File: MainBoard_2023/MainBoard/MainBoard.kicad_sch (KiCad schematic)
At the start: 27 parts

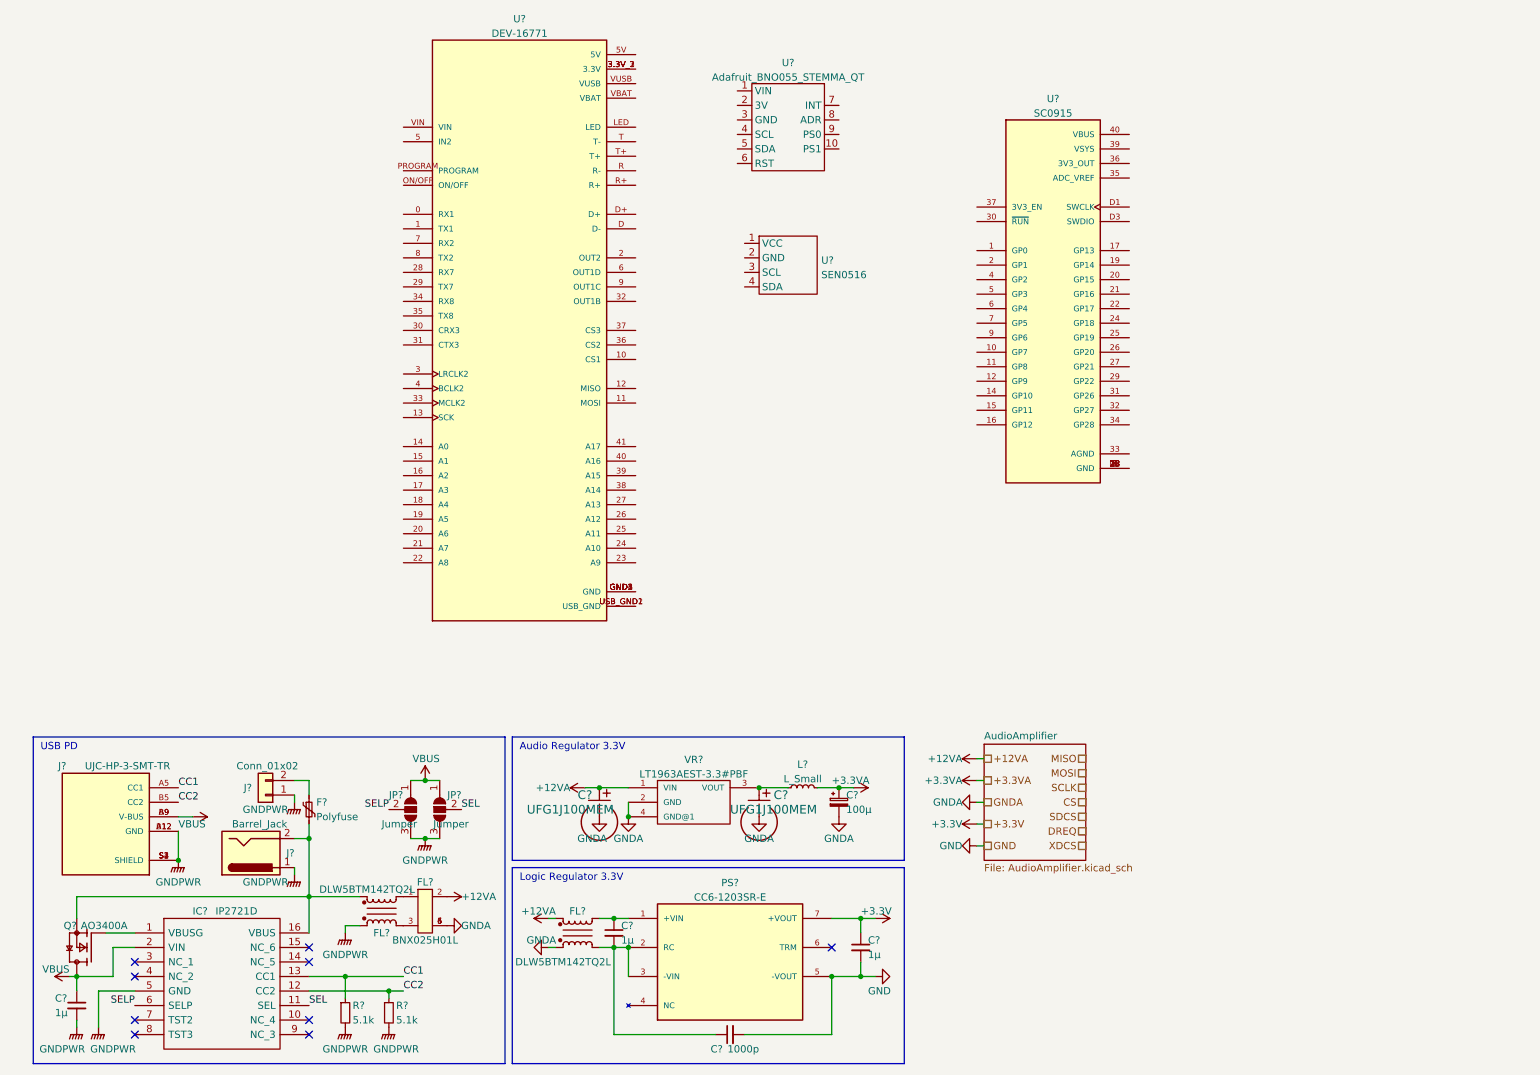
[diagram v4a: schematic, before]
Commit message: RS485回路を追加
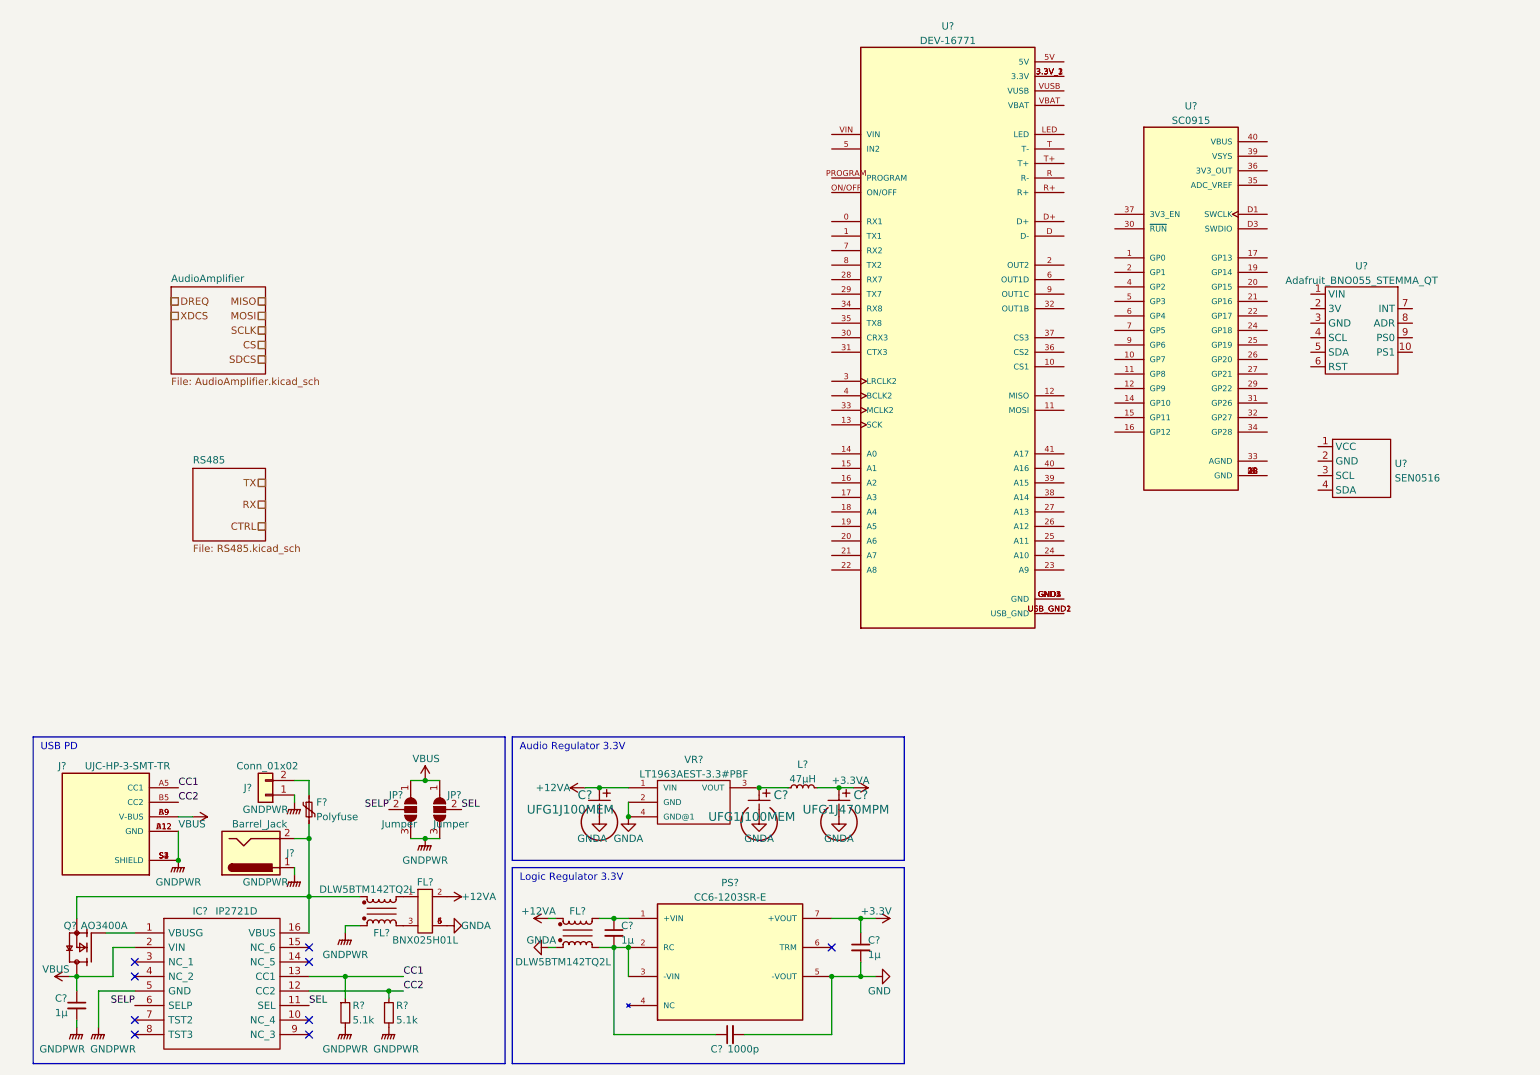
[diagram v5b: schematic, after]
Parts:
- removed C?: 100μ, symbol Device:C_Polarized_Small
- added C?: UFG1J470MPM, PCAP_10x12_5-THRU-ELECT_NCA, symbol UFG1J470MPM:UFG1J470MPM
- L?: value L_Small -> 47μH
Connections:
- net +3.3VA: now also C?.1
- net GNDA: now also C?.2
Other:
- added sheet RS485 (RS485.kicad_sch)
- moved on the sheet: U?

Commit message: picoのピンを設定
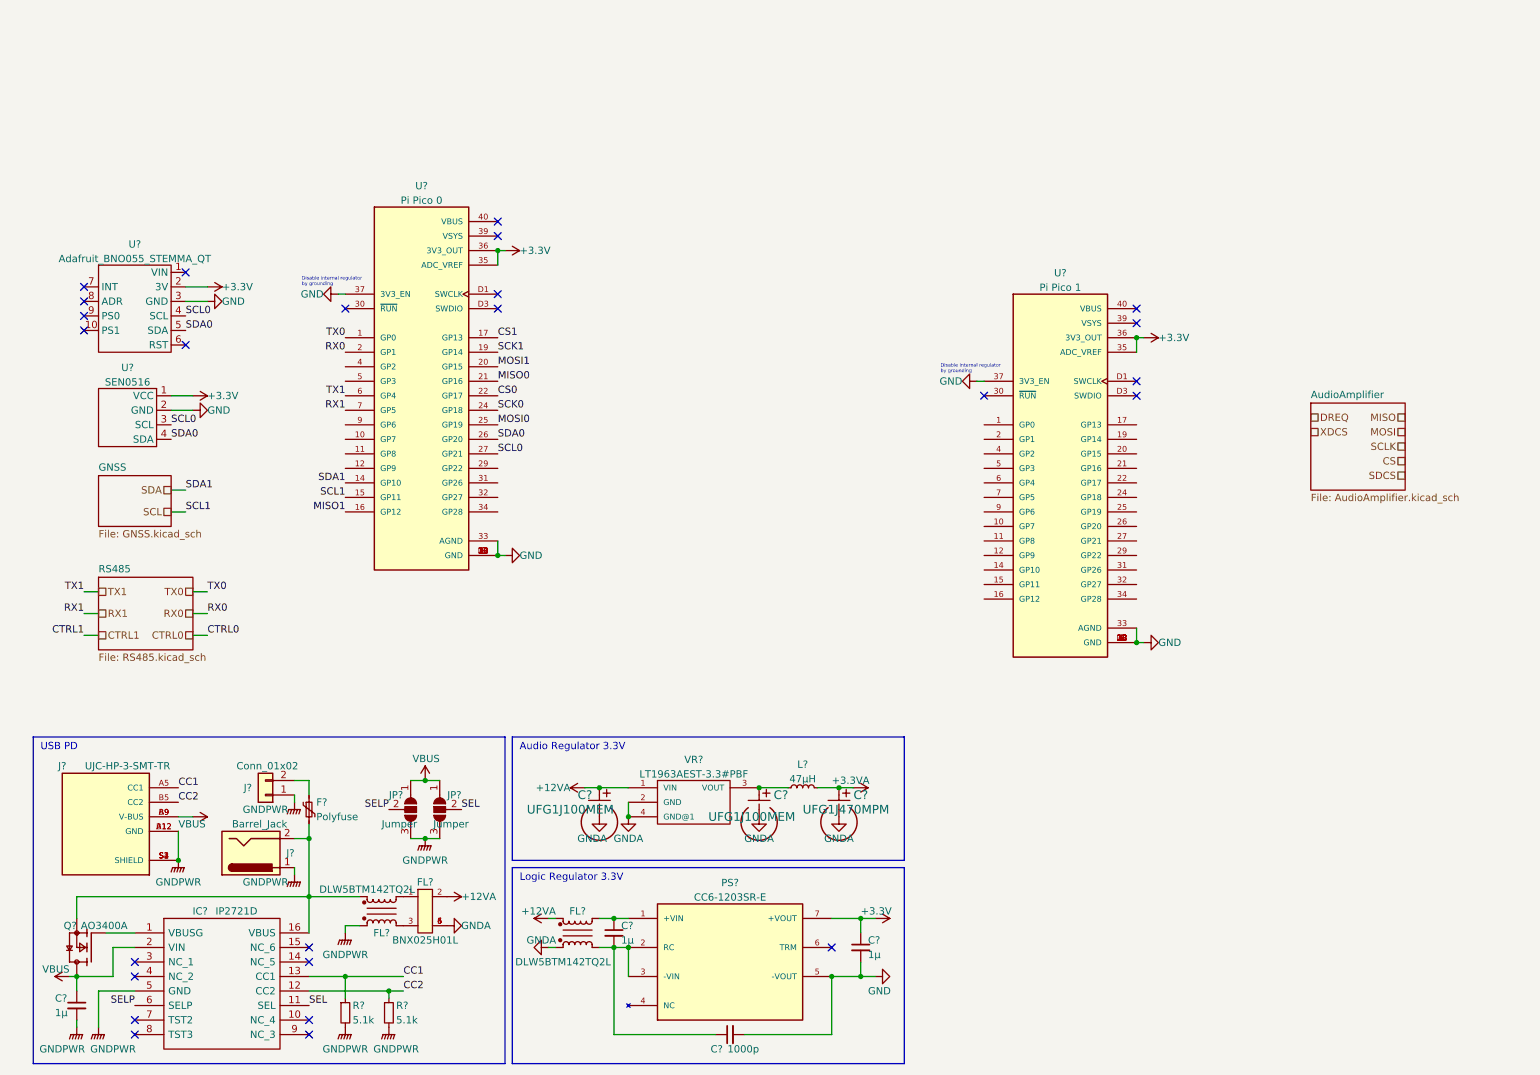
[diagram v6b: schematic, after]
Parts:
- removed U?: DEV-16771, MODULE_DEV-16771, symbol Teensy_4_1:DEV-16771
- removed U?: SC0915, MODULE_SC0915, symbol Raspberry_Pi_Pico:SC0915
- added U?: Pi Pico 0, MODULE_SC0915, symbol Raspberry_Pi_Pico:SC0915
- added U?: Pi Pico 1, MODULE_SC0915, symbol Raspberry_Pi_Pico:SC0915
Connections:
- net +3.3V: now also U?.1 (VCC), U?.2 (3V), U?.35 (ADC_VREF), U?.35 (ADC_VREF), U?.36 (3V3_OUT), U?.36 (3V3_OUT)
- net GND: now also U?.2 (GND), U?.3 (GND), U?.13 (GND), U?.13 (GND), U?.18 (GND), U?.18 (GND), U?.23 (GND), U?.23 (GND), U?.28 (GND), U?.28 (GND), U?.3 (GND), U?.3 (GND), U?.33 (AGND), U?.33 (AGND), U?.37 (3V3_EN), U?.37 (3V3_EN), U?.38 (GND), U?.38 (GND), U?.8 (GND), U?.8 (GND), U?.D2 (GND), U?.D2 (GND)
- net SCL0: now reaches U?.4 (SCL)
- net SCL0: now also U?.3 (SCL), U?.27 (GP21)
- net SDA0: now reaches U?.5 (SDA)
- net SDA0: now also U?.4 (SDA), U?.26 (GP20)
- new net CS0: U?.22 (GP17)
- new net CS1: U?.17 (GP13)
- new net MISO0: U?.21 (GP16)
- new net MISO1: U?.16 (GP12)
- new net MOSI0: U?.25 (GP19)
- new net MOSI1: U?.20 (GP15)
- new net RX0: U?.2 (GP1)
- new net RX1: U?.7 (GP5)
- new net SCK0: U?.24 (GP18)
- new net SCK1: U?.19 (GP14)
- new net SCL: U?.15 (GP11)
- new net SDA: U?.14 (GP10)
- new net TX0: U?.1 (GP0)
- new net TX1: U?.6 (GP4)
- no-connect marks 9 -> 25
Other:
- added sheet GNSS (GNSS.kicad_sch)
- note added: "Disable internal regulator by grounding"
- moved on the sheet: U?

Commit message: pico*2の場合
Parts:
- added C? (x2): 4.7μ, symbol Device:C_Small
- added C? (x2): 0.1μ, symbol Device:C_Small
- added J? (x2): Micro_SD_Card_Det_Hirose_DM3AT, symbol Connector:Micro_SD_Card_Det_Hirose_DM3AT
- added R? (x10): 10k, symbol Device:R_Small
- added R? (x2): 33, symbol Device:R_Small
- added U?: Seeed_Studio_XIAO_nRF52840_Sense, symbol Seeed_Studio_XIAO_nRF52840_Sense:Seeed_Studio_XIAO_nRF52840_Sense
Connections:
- net +3.3V: now also C?.1, C?.1, C?.1, C?.1, J?.4 (VDD), J?.4 (VDD), R?.2, R?.2, R?.2, R?.2, R?.2, R?.2, R?.2, R?.2, R?.2, R?.2, U?.12 (3V3)
- net CS0: now also J?.2 (DAT3/CD), R?.1
- net CTRL0: now also U?.4 (GP2)
- net CTRL1: now also U?.5 (GP3)
- net GND: now also C?.2, C?.2, C?.2, C?.2, J?.11 (SHIELD), J?.11 (SHIELD), J?.6 (VSS), J?.6 (VSS), U?.13 (GND)
- net MISO0: now also J?.7 (DAT0), R?.1
- net MOSI0: now also J?.3 (CMD), R?.1
- net SCK0: now also R?.1
- net RX2: now reaches U?.10 (GP7)
- net RX2: now also U?.7 (PB08_A6_D6_TX)
- net TX3: now reaches U?.11 (GP8)
- net TX3: now also U?.2 (GP1)
- net RX3: now reaches U?.12 (GP9)
- net RX3: now also U?.1 (GP0)
- net TX2: now reaches U?.9 (GP6)
- net TX2: now also U?.8 (PB09_A7_D7_RX)
- net MISO0_: now reaches U?.21 (GP16)
- net MISO0_: now also J?.7 (DAT0), R?.1
- net CS0_: now reaches U?.22 (GP17)
- net CS0_: now also J?.2 (DAT3/CD), R?.1
- net SCK0_: now reaches U?.24 (GP18)
- net SCK0_: now also R?.1
- net MOSI0_: now reaches U?.25 (GP19)
- net MOSI0_: now also J?.3 (CMD), R?.1
- new net: J?.8 (DAT1), R?.1 (x2)
- new net: J?.5 (CLK), R?.2 (x2)
- new net: J?.1 (DAT2), R?.1 (x2)
- no-connect marks 25 -> 43
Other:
- note added: "Audio"
- note added: "Interface"
- note added: "Measurement"
- note added: "SD Logging"
- moved on the sheet: C?, F?, FL?, IC?, J?, JP?, L?, PS?, Q?, R?, U?, VR?

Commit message: GNSSモジュール
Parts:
- removed U?: Pi Pico 1, MODULE_SC0915, symbol Raspberry_Pi_Pico:SC0915
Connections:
- net CS0_ is gone; now on net CS0: J?.2 (DAT3/CD), R?.1
- net MISO0_ is gone; now on net MISO0: J?.7 (DAT0), R?.1
- net MOSI0_ is gone; now on net MOSI0: J?.3 (CMD), R?.1
- net SCK0_ is gone; now on net SCK0: R?.1
- net CS0: no longer J?.2 (DAT3/CD), R?.1
- net CS1: now also J?.2 (DAT3/CD), R?.1
- net MISO0: no longer J?.7 (DAT0), R?.1
- net MISO1: now also J?.7 (DAT0), R?.1
- net MOSI0: no longer J?.3 (CMD), R?.1
- net MOSI1: now also J?.3 (CMD), R?.1
- net SCK0: no longer R?.1
- net SCK1: now also R?.1
- net RX2: no longer names the net of U?.10 (GP7), U?.7 (PB08_A6_D6_TX)
- net RX3: no longer names the net of U?.12 (GP9)
- net TX2: no longer names the net of U?.8 (PB09_A7_D7_RX), U?.9 (GP6)
- net TX3: no longer names the net of U?.11 (GP8)
- no-connect marks 43 -> 40
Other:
- moved on the sheet: U?
